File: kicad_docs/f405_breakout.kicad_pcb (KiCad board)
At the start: 4 copper layers, 50.8 x 83.8 mm, 38 parts, among them J1 DC_in, J2 SWD, J3 3.3v_out, J4 gnd_out, J5 port_A, J6 port_B, J7 port_C, U1 AMS1117-3.3, U2 STM32F405RGT6

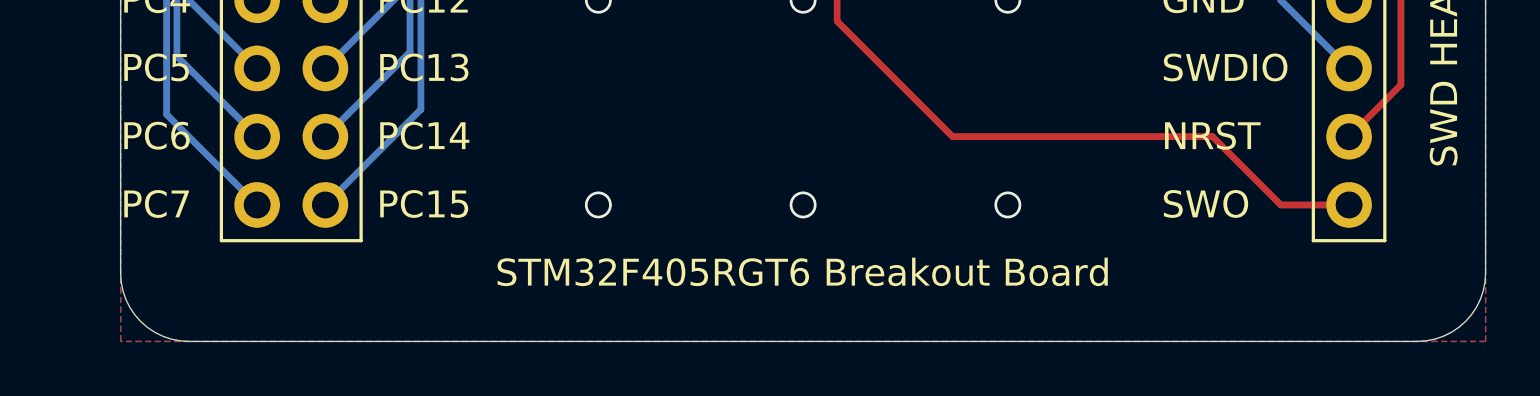
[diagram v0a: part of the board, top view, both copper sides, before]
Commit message: add git url to silkscreen
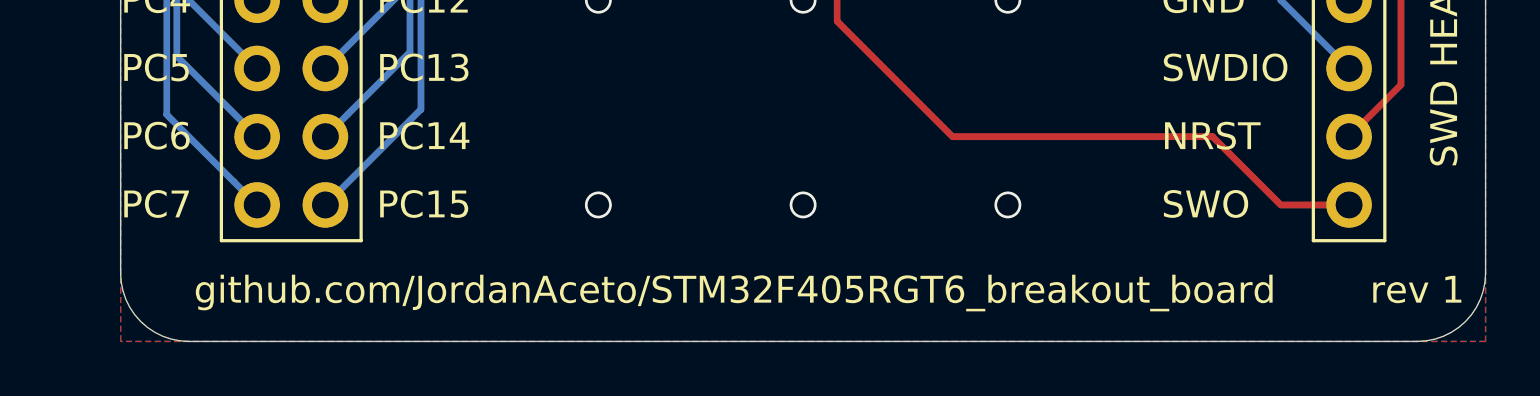
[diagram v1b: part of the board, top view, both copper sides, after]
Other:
- board text added: "github.com/JordanAceto/STM32F405RGT6_breakout_board"
- board text added: "rev 1"
- board text removed: "STM32F405RGT6 Breakout Board"
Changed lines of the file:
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@@
   (general
     (thickness 1.6)
-    (drawings 69)
+    (drawings 70)
     (tracks 774)
     (zones 0)
@@
     )
   )
-  (gr_text "STM32F405RGT6 Breakout Board" (at 127 132.08) (layer F.SilkS)
+  (gr_text "rev 1" (at 149.86 132.715) (layer F.SilkS)
     (effects (font (size 1 1) (thickness 0.15)))
   )
+  (gr_text github.com/JordanAceto/STM32F405RGT6_breakout_board (at 124.46 132.715) (layer F.SilkS)
+    (effects (font (size 1 1) (thickness 0.15)))
+  )
